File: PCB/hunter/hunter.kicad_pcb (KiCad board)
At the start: 2 copper layers, 36.2 x 52.6 mm, 29 parts, among them J1 Battery, J2 JTAG, SW1 SW_Light, SW2 SW_LightUp, SW3 SW_LightDown, SW4 SW_Fan, SW5 SW_FanUp, SW6 SW_FanDown, U1 CC1101RGPR, U2 STM8L101F3U6TR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

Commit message: second attempt
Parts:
- moved U2 22.6 mm to (81.8, 57.8), turned to 270 degrees
- moved C101 13.9 mm to (52.6, 53.2), turned to 90 degrees
- moved C124 12.8 mm to (52.0, 68.6), turned to 180 degrees
- moved R171 11.9 mm to (55.2, 62.0)
- moved C81 11.7 mm to (58.0, 53.2), turned to 90 degrees
- moved C131 10.1 mm to (54.8, 67.6)
- moved L121 10.1 mm to (52.8, 67.6)
- moved Y1 9.34 mm to (55.3, 53.2)
- moved J2 8.45 mm to (75.4, 52.4), turned to 90 degrees
- moved L131 8.05 mm to (54.4, 69.2)
- moved C121 7.94 mm to (53.4, 69.2)
- moved C61 7.78 mm to (76.4, 56.2), turned to 0 degrees
- moved L122 7.75 mm to (53.0, 71.2)
- moved C122 6.81 mm to (51.6, 71.8)
- moved U1 4.79 mm to (55.8, 58.0), turned to 180 degrees
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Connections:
- U1 pad V: GND -> (no net)
- U2 pad 10: Net-(SW1-Pad1) -> Net-(SW2-Pad1)
- U2 pad 18: Net-(U2-Pad18) -> Net-(D2-Pad2)
- U2 pad 2: Net-(D2-Pad2) -> Net-(U2-Pad2)
- U2 pad 3: Net-(SW3-Pad1) -> Net-(U2-Pad3)
- U2 pad 7: Net-(SW2-Pad1) -> Net-(SW1-Pad1)
- U2 pad 9: Net-(U2-Pad9) -> Net-(SW3-Pad1)
- Y1 pad 1: Net-(C81-Pad1) -> Net-(C101-Pad1)
- Y1 pad 2: Net-(C101-Pad1) -> Net-(C81-Pad1)
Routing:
- net Net-(D2-Pad2): track 25.5 -> 85.2 mm, vias 2 -> 0
- net GND: track 12.8 -> 43.9 mm, vias 3 -> 14
- net Net-(SW6-Pad1): track 12.4 -> 42.4 mm
- net Net-(SW5-Pad1): track 25.7 -> 54.7 mm
- net Net-(J2-Pad4): track 30.4 -> 3.99 mm, vias 2 -> 0
- net Net-(U1-Pad20): track 58.2 -> 34.4 mm, vias 6 -> 0
- net +3V0: track 93.4 -> 115.6 mm, vias 8 -> 4
- net Net-(AE1-Pad1): track 0.00 -> 21.8 mm
- net Net-(J2-Pad2): track 32.5 -> 12.3 mm
- net Net-(U1-Pad1): track 54.9 -> 35.2 mm, vias 6 -> 0
- net Net-(SW3-Pad1): track 26.1 -> 6.67 mm
- net Net-(C81-Pad1): track 20.9 -> 4.05 mm, vias 2 -> 0
- net Net-(SW1-Pad1): track 32.4 -> 17.0 mm
- net Net-(SW4-Pad1): track 15.1 -> 29.9 mm
- net Net-(D11-Pad2): track 21.1 -> 30.0 mm
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- added copper zone on B.Cu, net GND

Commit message: edits
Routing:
- net Net-(AE1-Pad1): track 21.8 -> 116.3 mm
- net +3V0: track 115.6 -> 114.4 mm
- net GND: vias 14 -> 13

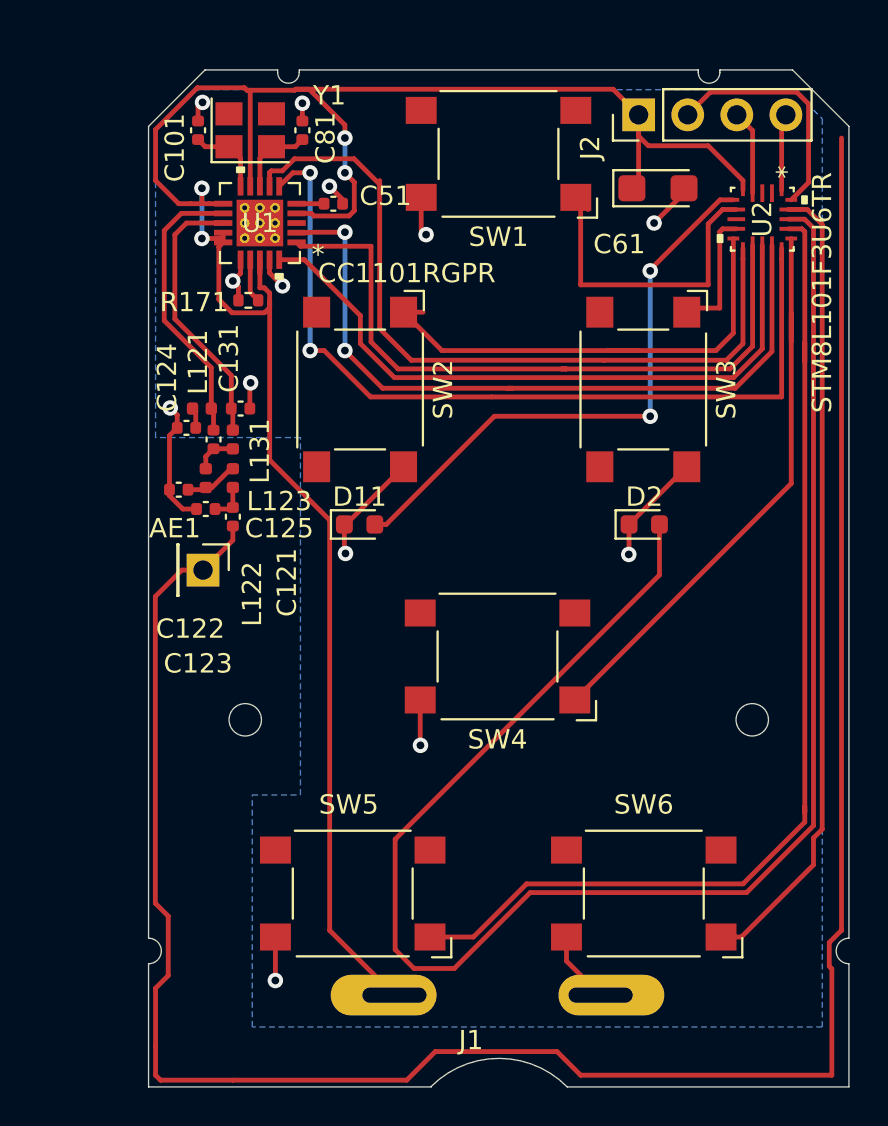
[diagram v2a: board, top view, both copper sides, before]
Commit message: Move the CPU to the middle, longer antenna, button pinout fix, wider holes
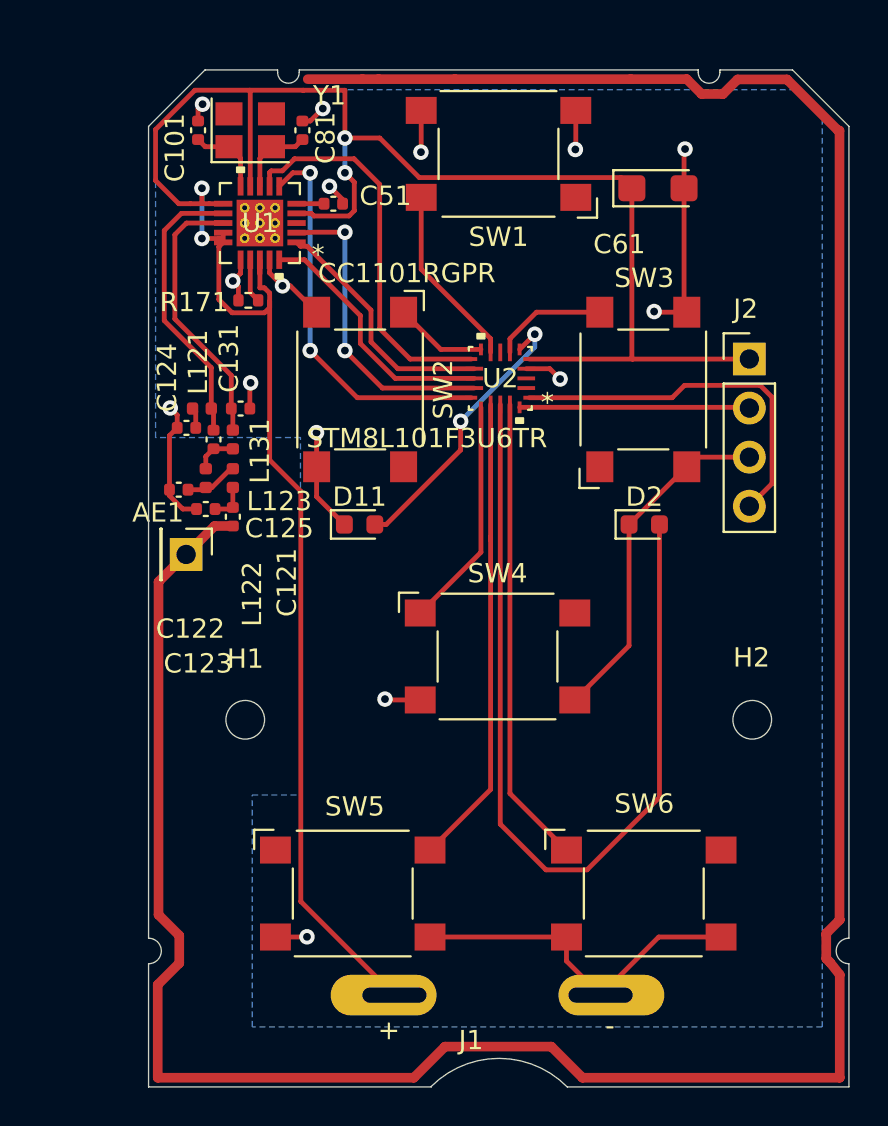
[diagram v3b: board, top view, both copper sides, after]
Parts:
- added H1: MountingHole, MountingHole:MountingHole_2mm, F.Cu at (55.0, 83.7)
- added H2: MountingHole, MountingHole:MountingHole_2mm, F.Cu at (81.2, 83.6)
- moved U2 15.9 mm to (68.2, 66.0), turned to 180 degrees
- moved J2 13.9 mm to (81.1, 65.0), turned to 0 degrees
- moved AE1 1.19 mm to (52.0, 75.1)
- turned SW3 to 90 degrees
- turned SW4 to 0 degrees
- turned SW5 to 0 degrees
- turned SW6 to 0 degrees
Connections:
- SW1 pad 2: GND -> Net-(SW1-Pad2)
- SW1 pad 3: (no net) -> GND
- SW1 pad 4: (no net) -> GND
- SW2 pad 2: GND -> Net-(SW2-Pad2)
- SW2 pad 3: (no net) -> GND
- SW2 pad 4: (no net) -> GND
- SW3 pad 2: GND -> Net-(SW3-Pad2)
- SW3 pad 3: (no net) -> GND
- SW3 pad 4: (no net) -> GND
- SW4 pad 2: GND -> Net-(SW4-Pad2)
- SW4 pad 3: (no net) -> GND
- SW4 pad 4: (no net) -> GND
- SW5 pad 2: GND -> Net-(SW5-Pad2)
- SW5 pad 3: (no net) -> GND
- SW5 pad 4: (no net) -> GND
- SW6 pad 2: GND -> Net-(SW6-Pad2)
- SW6 pad 3: (no net) -> GND
- SW6 pad 4: (no net) -> GND
- U2 pad 17: Net-(SW5-Pad1) -> Net-(SW5-Pad2)
- U2 pad 7: Net-(SW1-Pad1) -> Net-(SW3-Pad2)
- U2 pad 9: Net-(SW3-Pad1) -> Net-(SW1-Pad2)
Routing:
- net Net-(SW5-Pad1): track 54.7 -> 0.00 mm
- net Net-(D2-Pad2): track 85.2 -> 46.6 mm
- net GND: track 43.9 -> 79.2 mm, vias 13 -> 15
- net Net-(AE1-Pad1): track 116.3 -> 147.1 mm
- net Net-(SW5-Pad2): track 0.00 -> 24.5 mm
- net Net-(U1-Pad6): track 44.2 -> 20.4 mm
- net Net-(U1-Pad1): track 35.2 -> 12.9 mm
- net Net-(U1-Pad2): track 38.1 -> 16.1 mm
- net Net-(SW2-Pad1): track 25.8 -> 4.80 mm
- net Net-(U1-Pad20): track 34.4 -> 13.5 mm
- net Net-(U1-Pad7): track 39.7 -> 20.1 mm
- net Net-(SW6-Pad1): track 42.4 -> 24.3 mm
- net Net-(SW4-Pad1): track 29.9 -> 11.9 mm
- net Net-(SW1-Pad1): track 17.0 -> 0.00 mm
- net Net-(D11-Pad2): track 30.0 -> 14.7 mm
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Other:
- outline, holes or cut-outs redrawn

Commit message: correct the crystal. LCSC part numbers
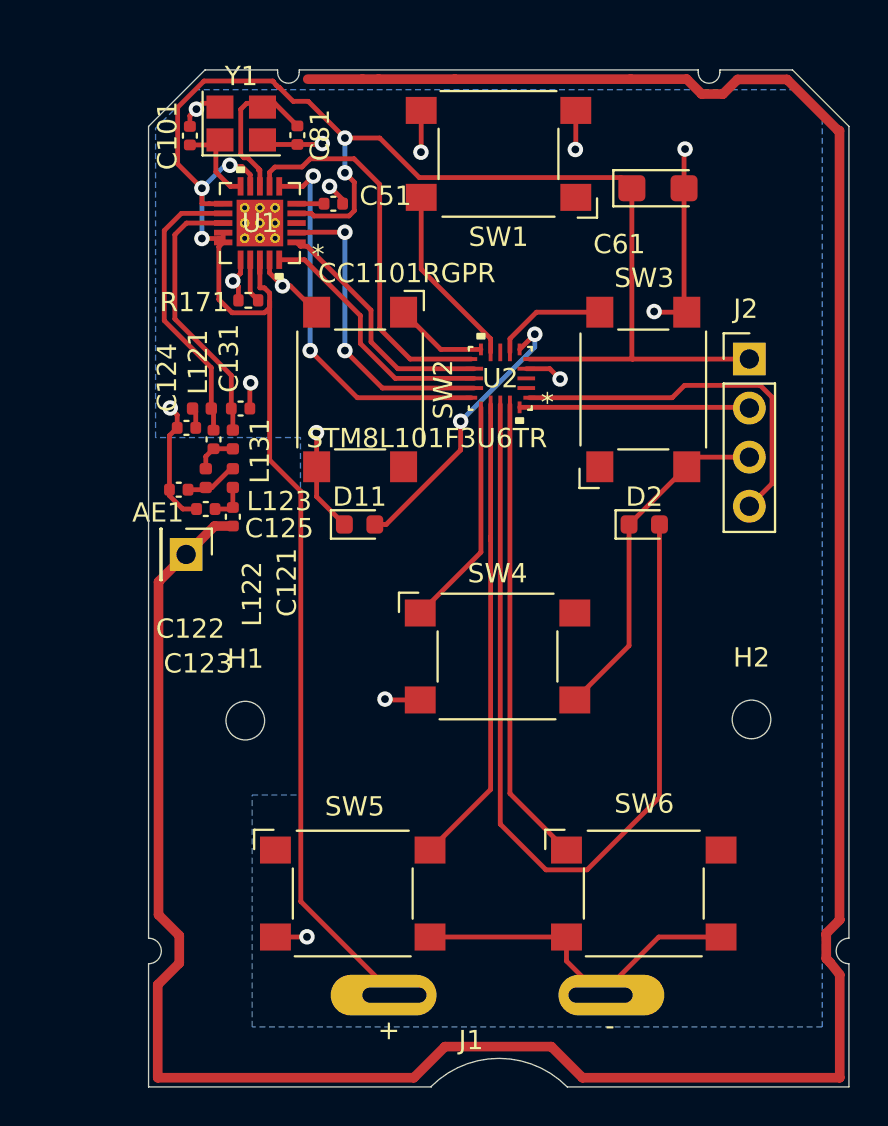
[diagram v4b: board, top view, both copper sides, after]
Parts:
- Y1: value 26MHz -> 25MHz
- moved Y1 0.58 mm to (54.8, 52.8)
- moved C101 0.51 mm to (52.2, 53.4)
- moved C81 0.36 mm to (57.7, 53.4)
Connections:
- C81 pad 1: Net-(C81-Pad1) -> GND
- C81 pad 2: GND -> Net-(C81-Pad2)
- U1 pad 8: Net-(C81-Pad1) -> Net-(C81-Pad2)
- Y1 pad 2: Net-(C81-Pad1) -> GND
- Y1 pad 3: (no net) -> Net-(C81-Pad2)
- Y1 pad 4: (no net) -> GND
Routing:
- net Net-(C81-Pad2): track 0.00 -> 8.10 mm
- net +3V0: track 121.3 -> 116.6 mm, vias 4 -> 5
- net Net-(C81-Pad1): track 4.05 -> 0.00 mm
- net GND: track 79.2 -> 82.6 mm
- net Net-(C101-Pad1): track 4.05 -> 5.46 mm

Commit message: no-op PCB change?
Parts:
- U1: value CC1101RGPR -> RGP20_2P4X2P4
- U2: value STM8L101F3U6TR -> UFQFPN20_3x3x0p6
